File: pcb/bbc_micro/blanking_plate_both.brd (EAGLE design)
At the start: 72.5 x 56 mm, 0 parts

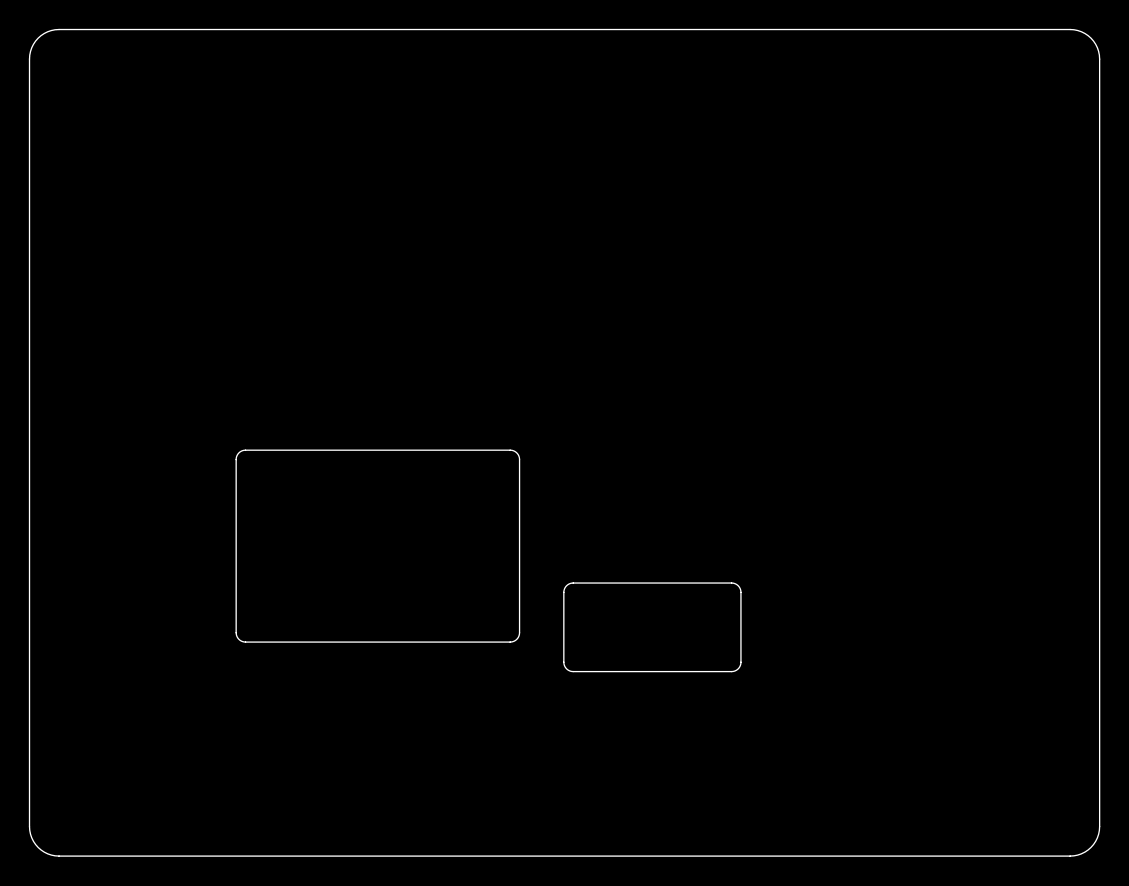
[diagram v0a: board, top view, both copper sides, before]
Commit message: test fit adjustment
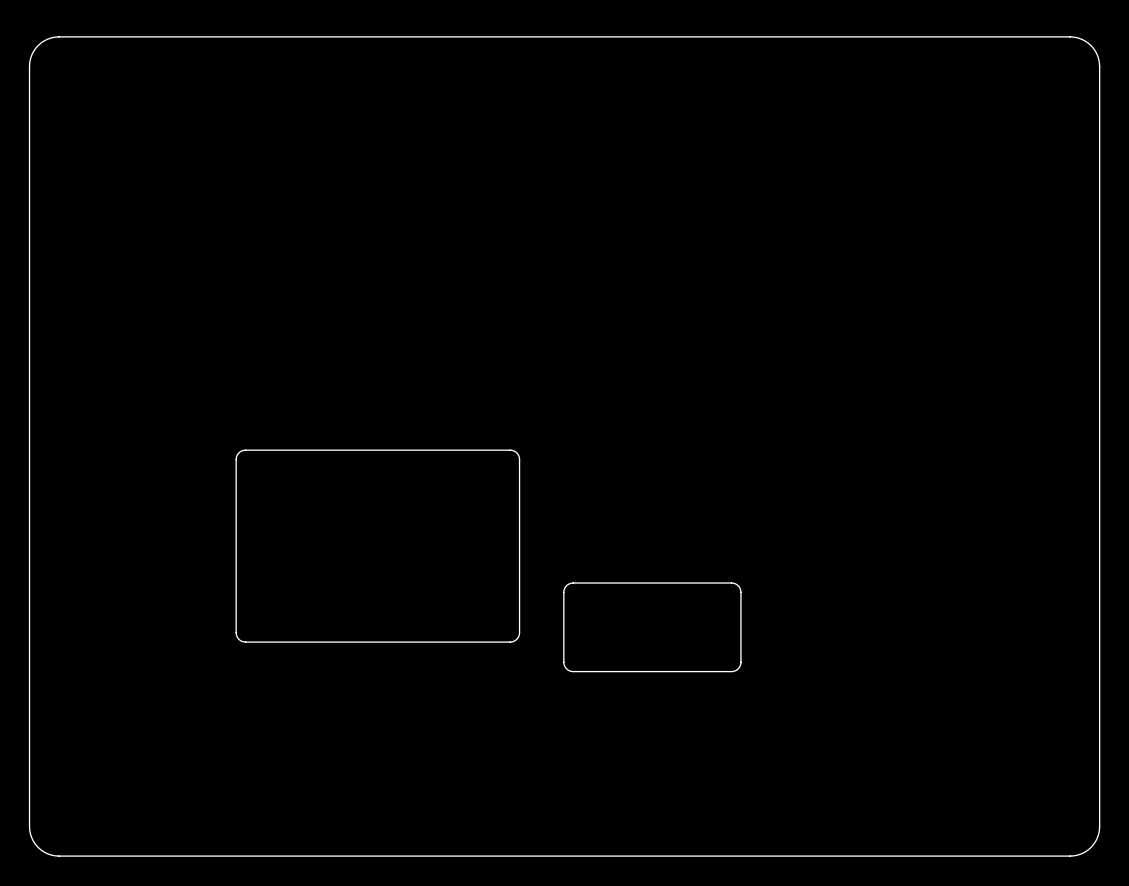
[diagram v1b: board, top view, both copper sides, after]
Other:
- board size 72.5 x 56 mm -> 72.5 x 55.5 mm
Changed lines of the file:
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@@
 <board>
 <plain>
-<wire x1="-2.5" y1="54" x2="-2.5" y2="2" width="0" layer="20"/>
+<wire x1="70" y1="2" x2="70" y2="53.5" width="0" layer="20"/>
+<wire x1="70" y1="53.5" x2="68" y2="55.5" width="0" layer="20" curve="90"/>
+<wire x1="68" y1="55.5" x2="-0.5" y2="55.5" width="0" layer="20"/>
+<wire x1="-0.5" y1="55.5" x2="-2.5" y2="53.5" width="0" layer="20" curve="90"/>
+<wire x1="-2.5" y1="53.5" x2="-2.5" y2="2" width="0" layer="20"/>
 <wire x1="-2.5" y1="2" x2="-0.5" y2="0" width="0" layer="20" curve="90"/>
 <wire x1="-0.5" y1="0" x2="68" y2="0" width="0" layer="20"/>
 <wire x1="68" y1="0" x2="70" y2="2" width="0" layer="20" curve="90"/>
-<wire x1="70" y1="2" x2="70" y2="54" width="0" layer="20"/>
-<wire x1="70" y1="54" x2="68" y2="56" width="0" layer="20" curve="90"/>
-<wire x1="68" y1="56" x2="-0.5" y2="56" width="0" layer="20"/>
-<wire x1="-0.5" y1="56" x2="-2.5" y2="54" width="0" layer="20" curve="90"/>
 <wire x1="30.7" y1="15.135" x2="30.7" y2="26.865" width="0" layer="20"/>
 <wire x1="30.7" y1="26.865" x2="30.065" y2="27.5" width="0" layer="20" curve="90"/>
